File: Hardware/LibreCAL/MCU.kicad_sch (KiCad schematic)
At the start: 30 parts, among them J5 USB_C_Receptacle_USB2.0, J6 TC2030-ARM, SW1 TL3301NF160QG, U5 W25Q16JVSNIQ, U6 IP4234CZ6, U7 RP2040, U8 W25Q128JVSIQ, Y1 ECS-120-8-36-CKM-TR3

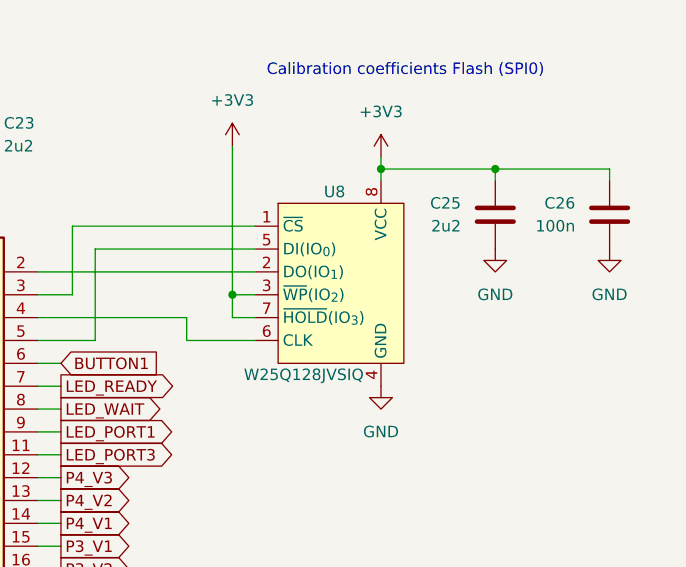
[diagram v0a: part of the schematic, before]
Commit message: Switch to W25N01GVZEIG 1Gbit flash
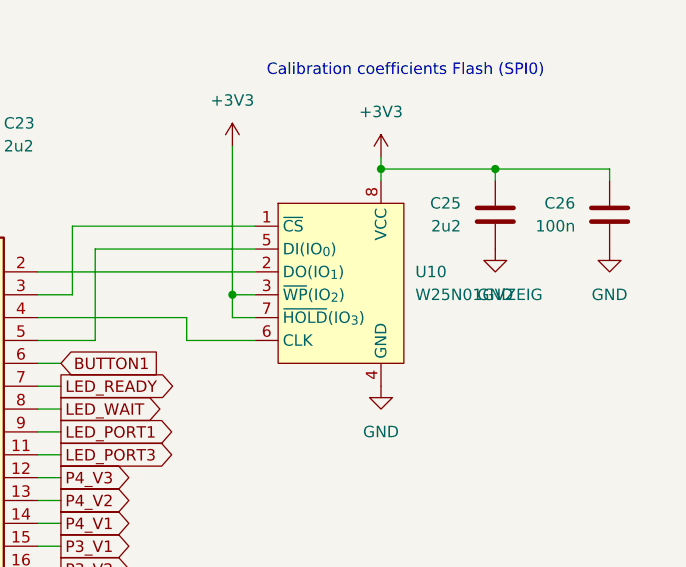
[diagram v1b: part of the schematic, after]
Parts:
- removed U8: W25Q128JVSIQ, Package_SO:SOIC-8_5.23x5.23mm_P1.27mm, symbol LibreCAL:W25Q16JVSNIQ
- added U10: W25N01GVZEIG, Package_SON:WSON-8-1EP_8x6mm_P1.27mm_EP3.4x4.3mm, symbol LibreCAL:W25N01GVZEIG
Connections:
- net +3V3: now also U10.3 (~{WP}(IO_{2})), U10.7 (~{HOLD}(IO_{3})), U10.8 (VCC)
- net GND: now also U10.4 (GND), U10.9 (GND)
- net at U7.2 (GPIO0): now also U10.2 (DO(IO_{1}))
- net at U7.3 (GPIO1): now also U10.1 (~{CS})
- net at U7.4 (GPIO2): now also U10.6 (CLK)
- net at U7.5 (GPIO3): now also U10.5 (DI(IO_{0}))
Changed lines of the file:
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@@
 	)
 	(symbol
+		(lib_id "LibreCAL:W25N01GVZEIG")
+		(at 237.49 72.39 0)
+		(unit 1)
+		(exclude_from_sim no)
+		(in_bom yes)
+		(on_board yes)
+		(dnp no)
+		(fields_autoplaced yes)
+		(property "Reference" "U10"
+			(at 243.84 72.3899 0)
+			(effects
+				(font
+					(size 1.27 1.27)
+				)
+				(justify left)
+			)
+		)
+		(property "Value" "W25N01GVZEIG"
+			(at 243.84 74.9299 0)
+			(effects
+				(font
+					(size 1.27 1.27)
+				)
+				(justify left)
+			)
+		)
+		(property "Footprint" "Package_SON:WSON-8-1EP_8x6mm_P1.27mm_EP3.4x4.3mm"
+			(at 237.49 72.39 0)
+			(effects
+				(font
+					(size 1.27 1.27)
+				)
+				(hide yes)
+			)
+		)
+		(property "Datasheet" ""
+			(at 237.49 72.39 0)
+			(effects
+				(font
+					(size 1.27 1.27)
+				)
+				(hide yes)
+			)
+		)
+		(property "Description" ""
+			(at 237.49 72.39 0)
+			(effects
+				(font
+					(size 1.27 1.27)
+				)
+				(hide yes)
+			)
+		)
+		(pin "2"
+		)
+		(pin "8"
+		)
+		(pin "1"
+		)
+		(pin "4"
+		)
+		(pin "3"
+		)
+		(pin "6"
+		)
+		(pin "5"
+		)
+		(pin "7"
+		)
+		(pin "9"
+		)
+		(instances
+			(project "LibreCAL"
+				(path "/b0788102-5488-43c5-b42c-71fadd77b28d/8ae04189-9a62-4c2c-b6af-68aaa5063c12"
+					(reference "U10")
+					(unit 1)
+				)
+			)
+		)
+	)
+	(symbol
 		(lib_id "Device:C")
 		(at 194.31 57.15 0)
@@
 					(unit 1)
 				)
-			)
-		)
-	)
-	(symbol
-		(lib_id "LibreCAL:W25Q16JVSNIQ")
-		(at 237.49 72.39 0)
-		(unit 1)
-		(exclude_from_sim no)
-		(in_bom yes)
-		(on_board yes)
-		(dnp no)
-		(property "Reference" "U8"
-			(at 233.68 63.4999 0)
-			(effects
-				(font
-					(size 1.27 1.27)
-				)
-				(justify left)
-			)
-		)
-		(property "Value" "W25Q128JVSIQ"
-			(at 224.79 83.8199 0)
-			(effects
-				(font
-					(size 1.27 1.27)
-				)
-				(justify left)
-			)
-		)
-		(property "Footprint" "Package_SO:SOIC-8_5.23x5.23mm_P1.27mm"
-			(at 237.49 72.39 0)
-			(effects
-				(font
-					(size 1.27 1.27)
-				)
-				(hide yes)
-			)
-		)
-		(property "Datasheet" "https://www.winbond.com/hq/support/documentation/levelOne.jsp?__locale=en&DocNo=DA00-W25Q16JV.1"
-			(at 237.49 72.39 0)
-			(effects
-				(font
-					(size 1.27 1.27)
-				)
-				(hide yes)
-			)
-		)
-		(property "Description" ""
-			(at 237.49 72.39 0)
-			(effects
-				(font
-					(size 1.27 1.27)
-				)
-				(hide yes)
-			)
-		)
-		(property "LCSC_Part" "C115407"
-			(at 237.49 72.39 0)
-			(effects
-				(font
-					(size 1.27 1.27)
-				)
-				(hide yes)
-			)
-		)
-		(pin "1"
-		)
-		(pin "2"
-		)
-		(pin "3"
-		)
-		(pin "4"
-		)
-		(pin "5"
-		)
-		(pin "6"
-		)
-		(pin "7"
-		)
-		(pin "8"
-		)
-		(instances
-			(project "LibreCAL"
-				(path "/b0788102-5488-43c5-b42c-71fadd77b28d/8ae04189-9a62-4c2c-b6af-68aaa5063c12"
-					(reference "U8")
-					(unit 1)
-				)

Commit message: Tweaks
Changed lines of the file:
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@@
 		(on_board yes)
 		(dnp no)
-		(fields_autoplaced yes)
 		(property "Reference" "U10"
-			(at 243.84 72.3899 0)
+			(at 242.824 78.994 0)
 			(effects
 				(font
@@
 		)
 		(property "Value" "W25N01GVZEIG"
-			(at 243.84 74.9299 0)
+			(at 242.824 81.534 0)
 			(effects
 				(font
@@
 		(on_board yes)
 		(dnp no)
-		(fields_autoplaced yes)
 		(property "Reference" "#PWR074"
 			(at 252.73 76.2 0)
